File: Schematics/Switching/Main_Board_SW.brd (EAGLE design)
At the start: 100 x 80 mm, 70 parts, among them Q1 32.768kHz, X1 MINI-USB-SHIELD-UX60-MB-5ST, X2 RJ45

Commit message: Button Updates
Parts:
- removed U$4: SPST, Switches_SPST:SPST
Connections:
- removed net N$45: U$1.P$41, U$4.A1, U$4.A2
- net +3V3: now also U$5.B1, U$5.B2, U$6.B1, U$6.B2
- net AGND: no longer U$4.B1, U$4.B2, U$5.B1, U$5.B2, U$6.B1, U$6.B2
- net N$41: now also U$1.P$34; no longer U$1.P$39
- net N$44: now also U$1.P$33; no longer U$1.P$38
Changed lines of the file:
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@@
 <element name="R27" library="rcl" package="R0805" value="373k" x="30.226" y="28.956"/>
 <element name="POWER_IN1" library="pinhead" package="1X02" value="6v" x="6.35" y="36.322"/>
-<element name="U$4" library="Switches_SPST" package="SPST" value="SPST" x="-57.15" y="30.48"/>
 <element name="U$5" library="Switches_SPST" package="SPST" value="SPST" x="-66.04" y="30.48"/>
 <element name="U$6" library="Switches_SPST" package="SPST" value="SPST" x="-74.93" y="30.48"/>
@@
 <wire x1="32.954" y1="23.876" x2="32.954" y2="27.178" width="0.254" layer="1"/>
 <wire x1="32.954" y1="27.178" x2="31.176" y2="28.956" width="0.254" layer="1"/>
+<contactref element="U$5" pad="B1"/>
+<contactref element="U$5" pad="B2"/>
+<contactref element="U$6" pad="B1"/>
+<contactref element="U$6" pad="B2"/>
+<wire x1="68.89876875" y1="38.14445" x2="68.89876875" y2="41.31945" width="0" layer="19" extent="1-1"/>
+<wire x1="68.89876875" y1="34.96945" x2="68.89876875" y2="38.14445" width="0" layer="19" extent="1-1"/>
+<wire x1="59.65063125" y1="35.60445" x2="68.89876875" y2="34.96945" width="0" layer="19" extent="1-1"/>
+<wire x1="59.65063125" y1="37.50945" x2="59.65063125" y2="35.60445" width="0" layer="19" extent="1-1"/>
+<wire x1="35.052" y1="23.114" x2="59.65063125" y2="35.60445" width="0" layer="19" extent="1-1"/>
+<wire x1="-21.91" y1="62.23" x2="22.86" y2="18.542" width="0" layer="19" extent="1-16"/>
+<wire x1="-34.61" y1="62.23" x2="-21.91" y2="62.23" width="0" layer="19" extent="1-1"/>
+<wire x1="-40.96" y1="62.23" x2="-34.61" y2="62.23" width="0" layer="19" extent="1-1"/>
+<wire x1="-21.195" y1="80.01" x2="-21.91" y2="62.23" width="0" layer="19" extent="1-1"/>
 <wire x1="-24.525" y1="80.01" x2="-21.195" y2="80.01" width="0" layer="19" extent="1-1"/>
 <wire x1="-29.605" y1="80.01" x2="-24.525" y2="80.01" width="0" layer="19" extent="1-1"/>
-<wire x1="-21.91" y1="62.23" x2="-21.195" y2="80.01" width="0" layer="19" extent="1-1"/>
-<wire x1="-34.61" y1="62.23" x2="-21.91" y2="62.23" width="0" layer="19" extent="1-1"/>
-<wire x1="-40.96" y1="62.23" x2="-34.61" y2="62.23" width="0" layer="19" extent="1-1"/>
-<wire x1="59.65063125" y1="37.50945" x2="-21.91" y2="62.23" width="0" layer="19" extent="1-1"/>
-<wire x1="59.65063125" y1="35.60445" x2="59.65063125" y2="37.50945" width="0" layer="19" extent="1-1"/>
-<wire x1="68.89876875" y1="38.14445" x2="59.65063125" y2="37.50945" width="0" layer="19" extent="1-1"/>
-<wire x1="68.89876875" y1="41.31945" x2="68.89876875" y2="38.14445" width="0" layer="19" extent="1-1"/>
-<wire x1="68.89876875" y1="34.96945" x2="68.89876875" y2="38.14445" width="0" layer="19" extent="1-1"/>
 <wire x1="-55.005" y1="80.01" x2="-40.96" y2="62.23" width="0" layer="19" extent="1-1"/>
 <wire x1="-60.085" y1="80.01" x2="-55.005" y2="80.01" width="0" layer="19" extent="1-1"/>
 <wire x1="-65.165" y1="80.01" x2="-60.085" y2="80.01" width="0" layer="19" extent="1-1"/>
 <wire x1="-69.29" y1="80.01" x2="-65.165" y2="80.01" width="0" layer="19" extent="1-1"/>
-<wire x1="-49.53" y1="1.27" x2="68.89876875" y2="34.96945" width="0" layer="19" extent="1-1"/>
-<wire x1="21.5265" y1="17.2085" x2="68.89876875" y2="41.31945" width="0" layer="19" extent="1-1"/>
+<wire x1="-61.49" y1="30.43" x2="-40.96" y2="62.23" width="0" layer="19" extent="1-1"/>
+<wire x1="-70.38" y1="30.43" x2="-61.49" y2="30.43" width="0" layer="19" extent="1-1"/>
+<wire x1="-70.43" y1="21.38" x2="-70.38" y2="30.43" width="0" layer="19" extent="1-1"/>
+<wire x1="-61.54" y1="21.38" x2="-70.43" y2="21.38" width="0" layer="19" extent="1-1"/>
+<wire x1="-49.53" y1="1.27" x2="-61.54" y2="21.38" width="0" layer="19" extent="1-1"/>
 </signal>
 <signal name="V+">
@@
 </signal>
 <signal name="AGND">
-<contactref element="U$4" pad="B1"/>
-<contactref element="U$4" pad="B2"/>
-<contactref element="U$5" pad="B1"/>
-<contactref element="U$5" pad="B2"/>
-<contactref element="U$6" pad="B1"/>
-<contactref element="U$6" pad="B2"/>
 <contactref element="C15" pad="1"/>
 <contactref element="C2" pad="1"/>
@@
 <contactref element="C14" pad="1"/>
 <contactref element="X2" pad="6"/>
-<wire x1="-61.54" y1="21.38" x2="-70.43" y2="21.38" width="0" layer="19" extent="1-1"/>
-<wire x1="-52.65" y1="21.38" x2="-61.54" y2="21.38" width="0" layer="19" extent="1-1"/>
-<wire x1="-70.38" y1="30.43" x2="-70.43" y2="21.38" width="0" layer="19" extent="1-1"/>
-<wire x1="-61.49" y1="30.43" x2="-70.38" y2="30.43" width="0" layer="19" extent="1-1"/>
-<wire x1="-52.6" y1="30.43" x2="-61.49" y2="30.43" width="0" layer="19" extent="1-1"/>
-<wire x1="-22.225" y1="17.907" x2="-52.65" y2="21.38" width="0" layer="19" extent="1-1"/>
-<wire x1="68.89876875" y1="45.12945" x2="-22.225" y2="17.907" width="0" layer="19" extent="1-1"/>
 <wire x1="59.65063125" y1="38.14445" x2="68.89876875" y2="45.12945" width="0" layer="19" extent="1-1"/>
-<wire x1="-35.14" y1="74.93" x2="59.65063125" y2="38.14445" width="0" layer="19" extent="1-1"/>
+<wire x1="-22.225" y1="17.907" x2="59.65063125" y2="38.14445" width="0" layer="19" extent="1-1"/>
+<wire x1="-35.14" y1="74.93" x2="-22.225" y2="17.907" width="0" layer="19" extent="1-1"/>
 <wire x1="-40.22" y1="74.93" x2="-35.14" y2="74.93" width="0" layer="19" extent="1-1"/>
 <wire x1="-36.435" y1="80.01" x2="-35.14" y2="74.93" width="0" layer="19" extent="1-1"/>
@@
 <wire x1="-28.575" y1="15.367" x2="59.65063125" y2="43.85945" width="0" layer="19" extent="1-1"/>
 </signal>
-<signal name="N$45">
-<contactref element="U$4" pad="A2"/>
-<contactref element="U$4" pad="A1"/>
-<contactref element="U$1" pad="P$41"/>
-<wire x1="-57.15" y1="30.48" x2="-57.15" y2="21.38" width="0" layer="19" extent="1-1"/>
-<wire x1="59.65063125" y1="41.31945" x2="-57.15" y2="30.48" width="0" layer="19" extent="1-1"/>
-</signal>
 <signal name="N$41">
 <contactref element="U$5" pad="A1"/>
-<contactref element="U$1" pad="P$39"/>
 <contactref element="U$5" pad="A2"/>
-<wire x1="-66.04" y1="30.48" x2="-66.04" y2="21.38" width="0" layer="19" extent="1-1"/>
-<wire x1="59.65063125" y1="40.68445" x2="-66.04" y2="30.48" width="0" layer="19" extent="1-1"/>
+<contactref element="U$1" pad="P$34"/>
+<wire x1="-66.04" y1="30.48" x2="59.65063125" y2="36.87445" width="0" layer="19" extent="1-1"/>
+<wire x1="-66.04" y1="21.38" x2="-66.04" y2="30.48" width="0" layer="19" extent="1-1"/>
 </signal>
 <signal name="N$44">
 <contactref element="U$6" pad="A2"/>
 <contactref element="U$6" pad="A1"/>
-<contactref element="U$1" pad="P$38"/>
-<wire x1="-74.93" y1="30.48" x2="-74.93" y2="21.38" width="0" layer="19" extent="1-1"/>
-<wire x1="59.65063125" y1="39.41445" x2="-74.93" y2="30.48" width="0" layer="19" extent="1-1"/>
+<contactref element="U$1" pad="P$33"/>
+<wire x1="-74.93" y1="30.48" x2="59.65063125" y2="36.23945" width="0" layer="19" extent="1-1"/>
+<wire x1="-74.93" y1="21.38" x2="-74.93" y2="30.48" width="0" layer="19" extent="1-1"/>
 </signal>
 <signal name="N$43">

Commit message: Stuff
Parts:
- added C10, C31: 47uF, rcl:C1210
- added C11, C32: 1uF, rcl:C0603
- added C12, C9: 1000pF, rcl:C0402
- added C7, C8: 0.047uF, rcl:C0402
- added R8, R9: 2, rcl:R0402
- D5, D6, D7, D8: value 1N5818-T -> (none); device diode:DO41-7.6 -> diode:SOD323-R
- ISP: device pinhead:2X05/90 -> con-samtec:FTSH-105-01-L-DV-K
- R16: value 200k -> 499K
- R19: value 200k -> 499k
- moved Z3 165.4 mm to (88.1, 22.1), turned to 90 degrees
- moved Z2 151.3 mm to (81.5, 24.1), turned to 90 degrees
- moved C13 148.7 mm to (92.7, 14.2), turned to 180 degrees
- moved Z1 148.4 mm to (85.1, 21.3), turned to 90 degrees
- moved C18 146.0 mm to (72.9, 35.1), turned to 180 degrees
- moved U$7 145.2 mm to (59.7, 19.8)
- moved C17 139.3 mm to (72.9, 41.4), turned to 180 degrees
- moved R5 138.6 mm to (84.6, 31.2), turned to 90 degrees
- moved Q1 137.8 mm to (88.6, 44.7)
- moved X1 131.8 mm to (95.0, 27.4), turned to 180 degrees
- moved R4 130.0 mm to (80.5, 35.1), turned to 180 degrees
- moved R7 124.0 mm to (65.5, 22.4), turned to 90 degrees
- moved U$6 123.9 mm to (48.8, 24.1), turned to 270 degrees
- moved R13 122.1 mm to (80.0, 55.9)
- moved C16 120.1 mm to (55.4, 34.8)
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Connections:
- removed net AGND: C14.1, C15.1, C2.1, C3.1, C6.1, U$1.P$23, U$1.P$36, X2.6
- removed net N$21: R12.1, U$1.P$18, X2.8
- new net N$130: C9.2, R8.2
- new net N$131: C12.2, R9.2
- new net N$61: R13.1, U$1.P$19, X2.2
- net +3V3: now also C32.1, D5.C
- net +5V: now also C11.1, D6.C, X2.4; no longer X2.5
- net ANALOGINPUT: now also X2.8; no longer X2.2
- net GND: now also C10.2, C11.2, C14.1, C15.1, C2.1, C3.1, C31.2, C32.2, C6.1, C7.2, C8.2, D7.A, D8.A, R8.1, R9.1, U$1.P$23, U$1.P$36, X2.3
- net N$18: now also X2.5; no longer X2.3
- net N$19: now also X2.6; no longer X2.4
- net N$20: now also R12.1, U$1.P$18, X2.1; no longer R13.1, U$1.P$19, X2.7
- net N$25: now also C7.1
- net N$26: now also C9.1
- net N$28: now also D6.A; no longer D6.C
- net N$32: now also C8.1
- net N$34: now also C12.1
- net N$35: now also D5.A; no longer D5.C
- net N$42: now also X2.7; no longer X2.1
- net V+: now also C10.1, C31.1; no longer D5.A, D6.A, D7.A, D8.A
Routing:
- net GND: track 175.9 -> 444.2 mm, vias 17 -> 38
- net +3V3: track 28.3 -> 218.2 mm, vias 2 -> 9
- net +5V: track 30.1 -> 124.5 mm, vias 2 -> 6
- net N$20: track 0.00 -> 47.9 mm, vias 0 -> 1
- net N$61: track 0.00 -> 42.7 mm, vias 0 -> 3
- net ANALOGINPUT: track 0.00 -> 41.5 mm
- net PE: track 0.00 -> 37.2 mm, vias 0 -> 2
- net N$42: track 0.00 -> 36.6 mm, vias 0 -> 3
- net N$16: track 0.00 -> 36.2 mm, vias 0 -> 2
- net N$18: track 0.00 -> 33.6 mm, vias 0 -> 2
- net N$23: track 0.00 -> 32.2 mm, vias 0 -> 2
- net N$14: track 0.00 -> 30.2 mm, vias 0 -> 4
- net N$44: track 0.00 -> 27.4 mm, vias 0 -> 2
- net N$3: track 0.00 -> 21.5 mm, vias 0 -> 2
- net N$19: track 0.00 -> 21.3 mm
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
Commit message: Switching Layout Placed
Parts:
- moved C9 94.4 mm to (16.1, 72.2), turned to 180 degrees
- moved R8 87.8 mm to (11.4, 72.2)
- moved C32 86.2 mm to (29.1, 27.4), turned to 180 degrees
- moved C11 82.8 mm to (27.4, 45.9), turned to 180 degrees
- moved C10 78.4 mm to (14.2, 51.0)
- moved C31 74.4 mm to (10.9, 25.7), turned to 90 degrees
- moved C7 73.1 mm to (25.7, 66.2)
- moved R9 53.7 mm to (26.9, 4.95), turned to 180 degrees
- moved C12 48.0 mm to (23.6, 4.95)
- moved C8 22.6 mm to (12.9, 10.7), turned to 180 degrees
- moved D8 4.90 mm to (21.8, 3.61)
- moved D6 4.19 mm to (15.3, 66.3)
- moved D5 3.21 mm to (24.8, 8.47)
- moved R24 3.00 mm to (23.5, 31.5)
- moved R22 2.75 mm to (13.2, 46.9)
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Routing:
- net GND: track 444.2 -> 503.8 mm, vias 38 -> 123
- net V+: track 235.8 -> 208.1 mm, vias 13 -> 10
- net +5V: track 124.5 -> 144.2 mm, vias 6 -> 8
- net +3V3: track 218.2 -> 233.6 mm, vias 9 -> 12
- net N$26: track 6.99 -> 18.8 mm
- net N$35: track 12.6 -> 5.76 mm
- net N$32: track 3.48 -> 9.50 mm
- net N$38: track 36.6 -> 40.2 mm
- net N$130: track 0.00 -> 3.42 mm
- net N$30: track 43.3 -> 40.7 mm, vias 3 -> 4
- net N$25: track 8.64 -> 10.9 mm
- net N$131: track 0.00 -> 2.05 mm
- net N$34: track 12.2 -> 10.6 mm

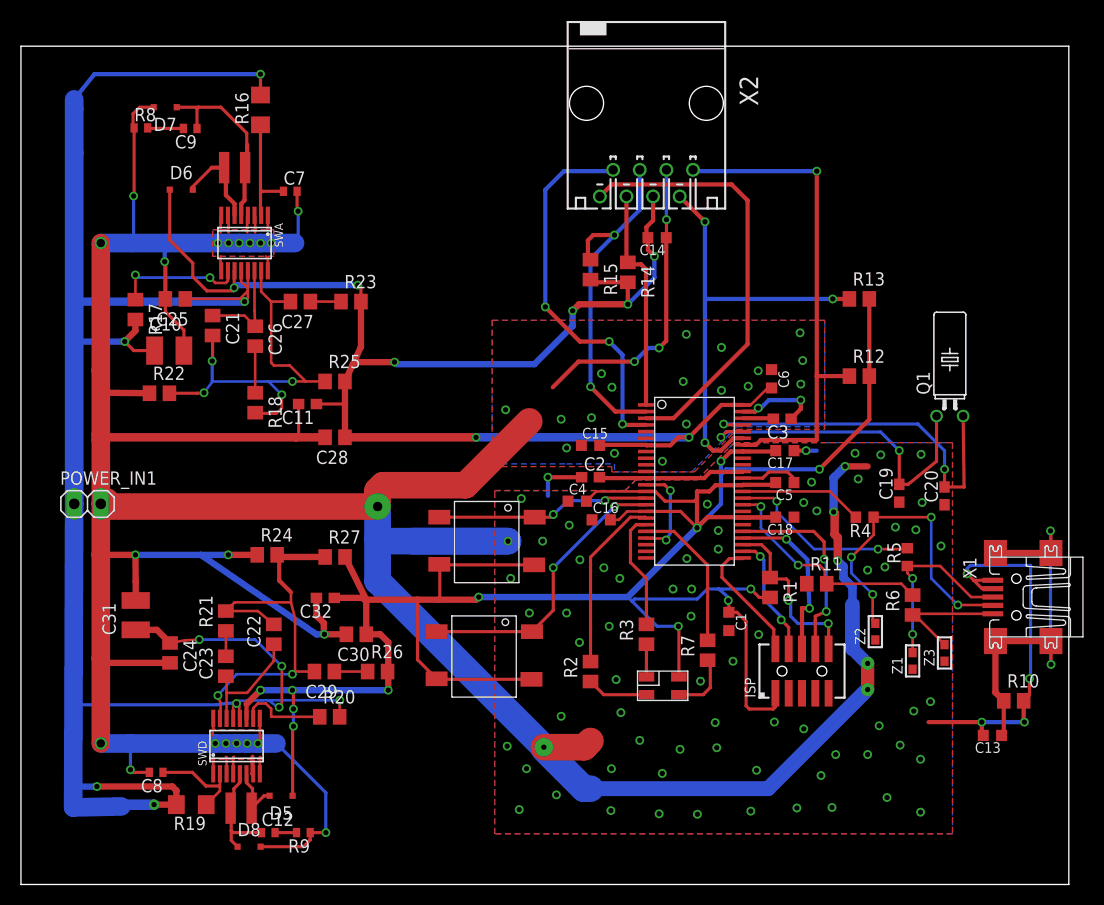
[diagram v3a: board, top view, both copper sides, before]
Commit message: Added Drill Holes. Moved Traces. Moved Silkscreen References
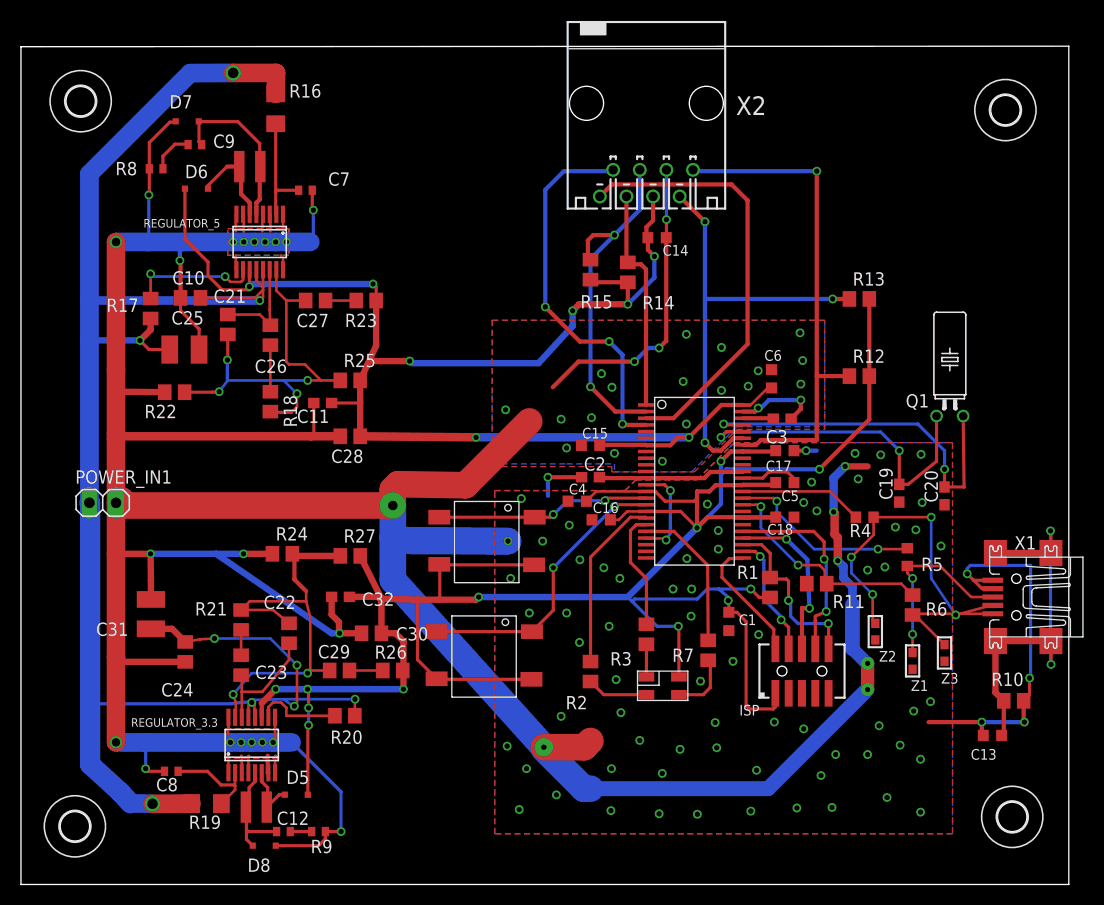
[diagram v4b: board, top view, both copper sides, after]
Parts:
- removed SWA, SWD: SWITCHER, linear-technology-2:SSOP16
- added H1, H2, H3, H4: MOUNT-HOLE2.8, holes:2,8
- added REGULATOR_3.3, REGULATOR_5: SWITCHER, linear-technology-2:SSOP16
- moved R8 4.16 mm to (12.9, 68.3)
- moved D7 2.50 mm to (15.9, 72.8)
- moved C9 1.61 mm to (16.6, 70.6)
- moved R20 1.45 mm to (30.9, 16.1)
- moved R24 1.45 mm to (24.9, 31.6)
- moved C30 1.45 mm to (33.5, 24.0)
- moved C31 1.45 mm to (12.4, 25.8)
- moved POWER_IN1 1.45 mm to (7.80, 36.4)
- moved R16 1.45 mm to (24.3, 74.0)
- moved C11 1.45 mm to (28.8, 46.0)
- moved C23 1.45 mm to (21.0, 20.9)
- moved C24 1.45 mm to (15.7, 22.2)
- moved C26 1.45 mm to (23.8, 52.4)
- moved C27 1.45 mm to (28.1, 55.7)
- moved C28 1.45 mm to (31.4, 42.8)
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- renumbered U$7 to RGB_LED
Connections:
- net +3V3: now also REGULATOR_3.3.11; no longer SWD.11
- net +5V: now also REGULATOR_5.11; no longer SWA.11
- net GND: now also REGULATOR_3.3.1, REGULATOR_3.3.16, REGULATOR_3.3.3, REGULATOR_3.3.4, REGULATOR_3.3.7, REGULATOR_3.3.8, REGULATOR_3.3.9, REGULATOR_5.1, REGULATOR_5.16, REGULATOR_5.3, REGULATOR_5.4, REGULATOR_5.7, REGULATOR_5.8, REGULATOR_5.9; no longer SWA.1, SWA.16, SWA.3, SWA.4, SWA.7, SWA.8, SWA.9, SWD.1, SWD.16, SWD.3, SWD.4, SWD.7, SWD.8, SWD.9
- net N$24: now also REGULATOR_5.14; no longer SWA.14
- net N$25: now also REGULATOR_5.2; no longer SWA.2
- net N$26: now also REGULATOR_5.5; no longer SWA.5
- net N$27: now also REGULATOR_5.10; no longer SWA.10
- net N$28: now also REGULATOR_5.6; no longer SWA.6
- net N$30: now also REGULATOR_5.15; no longer SWA.15
- net N$32: now also REGULATOR_3.3.2; no longer SWD.2
- net N$33: now also REGULATOR_3.3.10; no longer SWD.10
- net N$34: now also REGULATOR_3.3.5; no longer SWD.5
- net N$35: now also REGULATOR_3.3.6; no longer SWD.6
- net N$36: now also REGULATOR_3.3.14; no longer SWD.14
- net N$38: now also REGULATOR_3.3.15; no longer SWD.15
- net V+: now also REGULATOR_3.3.12, REGULATOR_3.3.13, REGULATOR_5.12, REGULATOR_5.13; no longer SWA.12, SWA.13, SWD.12, SWD.13
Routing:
- net V+: track 208.1 -> 186.8 mm, vias 10 -> 9
- net GND: track 503.8 -> 498.2 mm
- net +5V: track 144.2 -> 141.3 mm
- net N$26: track 18.8 -> 16.0 mm
- net +3V3: track 233.6 -> 232.1 mm
- net N$14: track 30.2 -> 31.2 mm
- net N$130: track 3.42 -> 4.10 mm
